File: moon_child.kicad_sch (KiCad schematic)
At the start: 0 parts

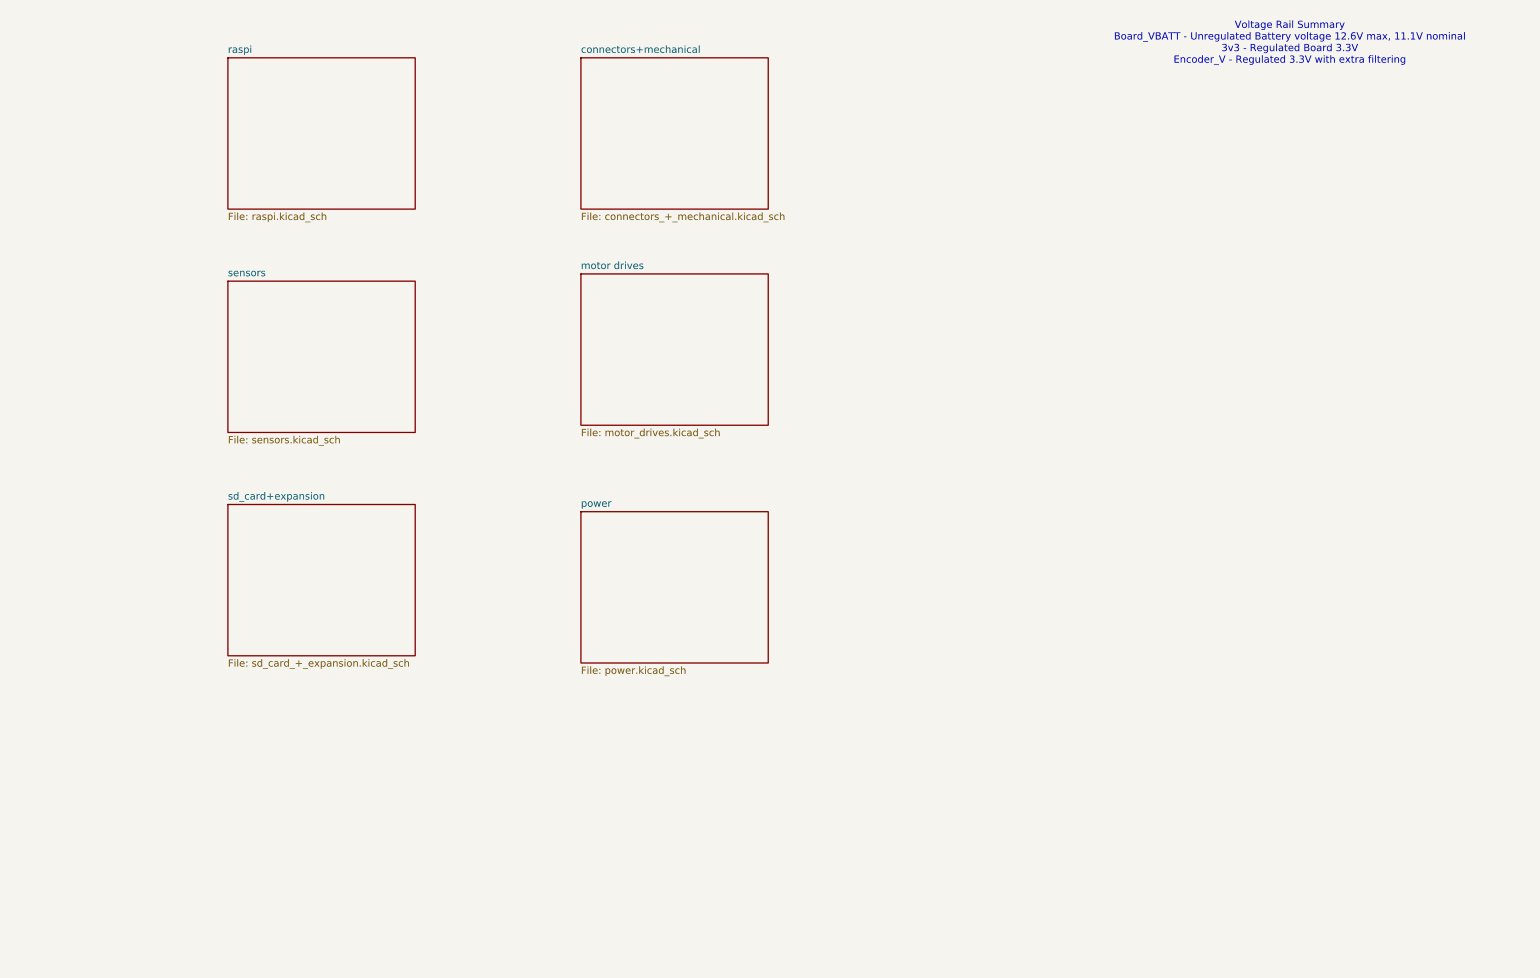
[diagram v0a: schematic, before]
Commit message: Setup top sheet
Added TVS diodes, updated top sheet, misc label fixes
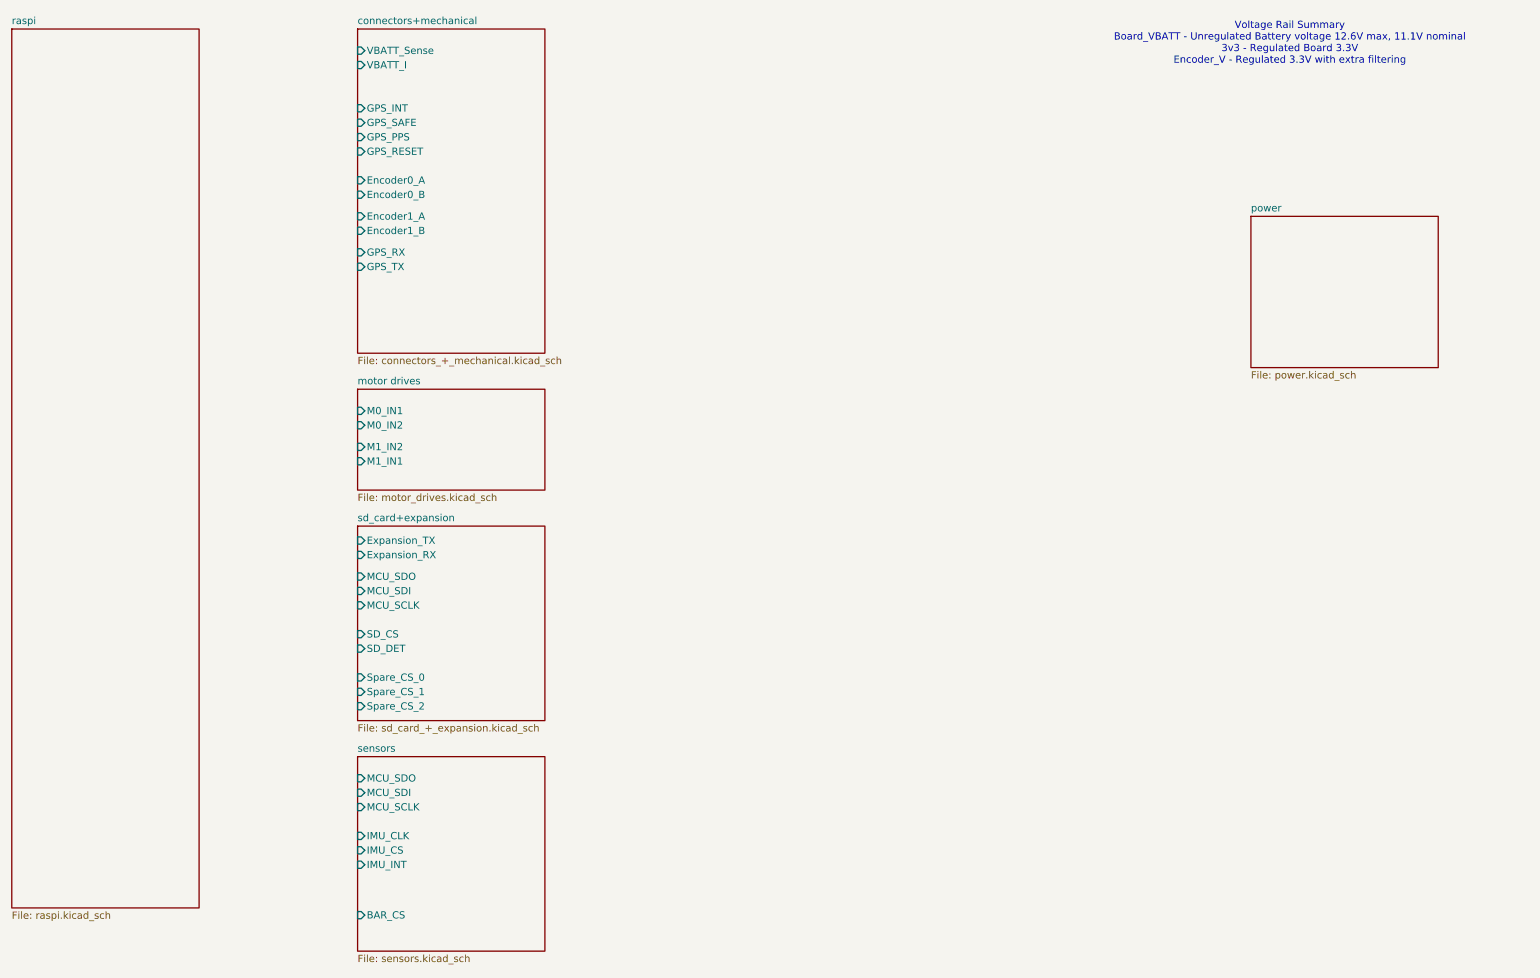
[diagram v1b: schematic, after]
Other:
- sheet connectors+mechanical ports: added Encoder0_A, Encoder0_B, Encoder1_A, Encoder1_B, GPS_INT, GPS_PPS, GPS_RESET, GPS_RX, GPS_SAFE, GPS_TX, VBATT_I, VBATT_Sense; removed none
- sheet motor drives ports: added M0_IN1, M0_IN2, M1_IN1, M1_IN2; removed none
- sheet sd_card+expansion ports: added Expansion_RX, Expansion_TX, MCU_SCLK, MCU_SDI, MCU_SDO, SD_CS, SD_DET, Spare_CS_0, Spare_CS_1, Spare_CS_2; removed none
- sheet sensors ports: added BAR_CS, IMU_CLK, IMU_CS, IMU_INT, MCU_SCLK, MCU_SDI, MCU_SDO; removed none

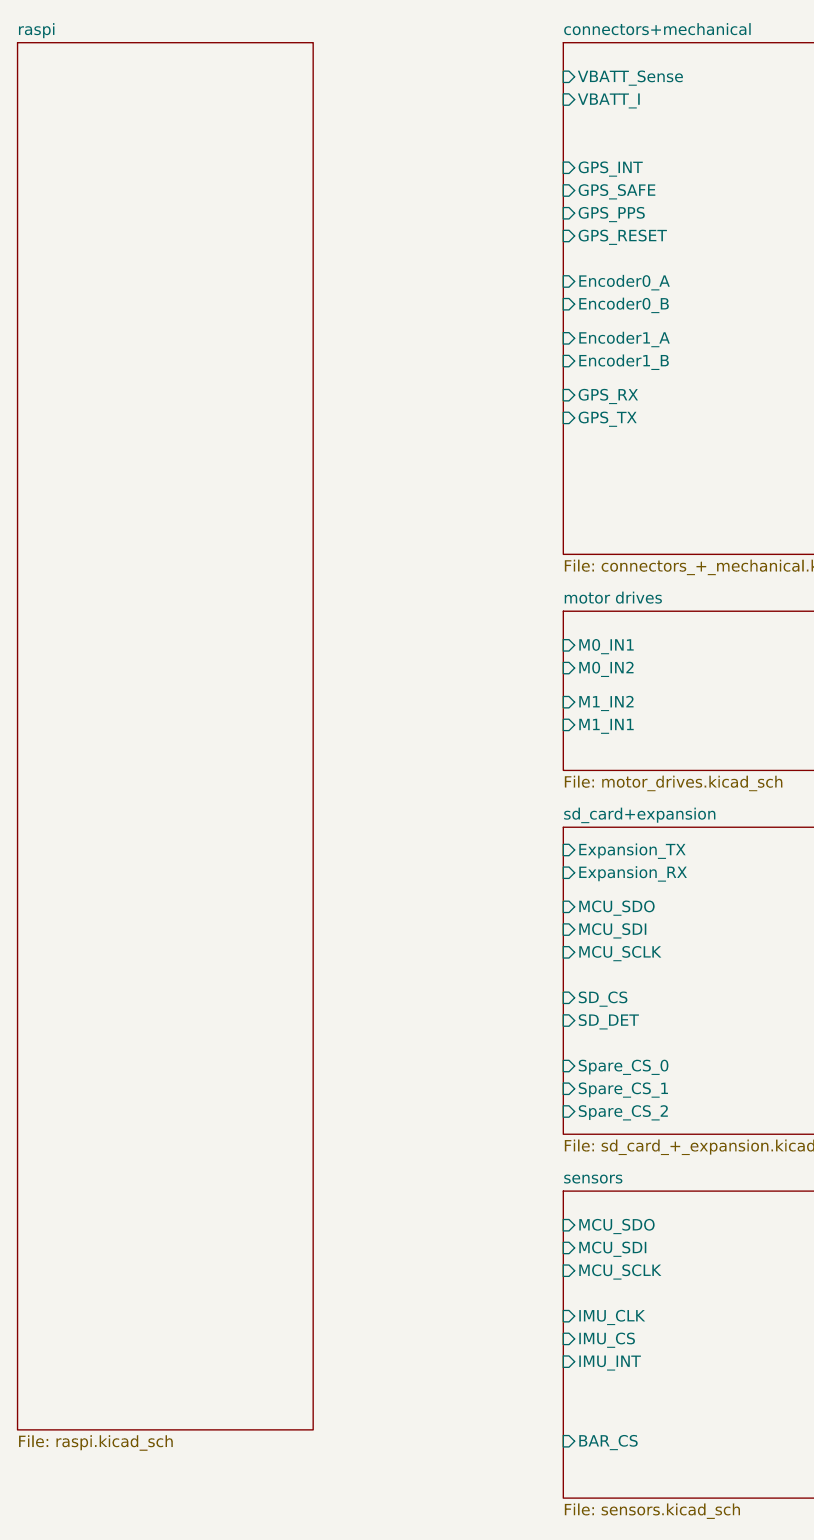
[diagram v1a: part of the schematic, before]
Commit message: Updated sheet to sheet pinout
Updated pinouts and cleared ERCs
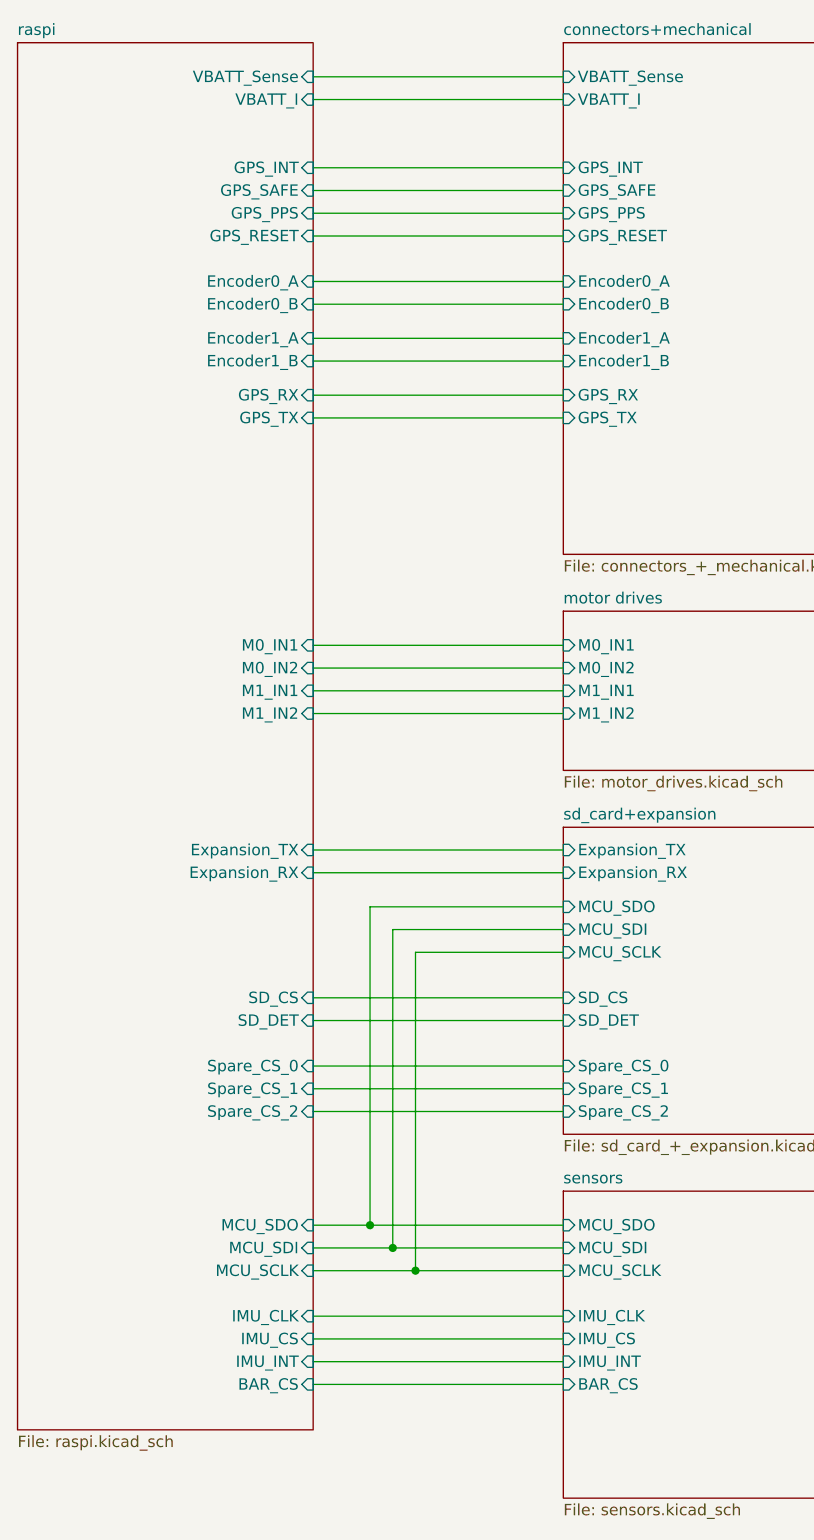
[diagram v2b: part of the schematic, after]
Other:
- sheet raspi ports: added BAR_CS, Encoder0_A, Encoder0_B, Encoder1_A, Encoder1_B, Expansion_RX, Expansion_TX, GPS_INT, GPS_PPS, GPS_RESET, GPS_RX, GPS_SAFE, GPS_TX, IMU_CLK, IMU_CS, IMU_INT, M0_IN1, M0_IN2, M1_IN1, M1_IN2, MCU_SCLK, MCU_SDI, MCU_SDO, SD_CS, SD_DET, Spare_CS_0, Spare_CS_1, Spare_CS_2, VBATT_I, VBATT_Sense; removed none

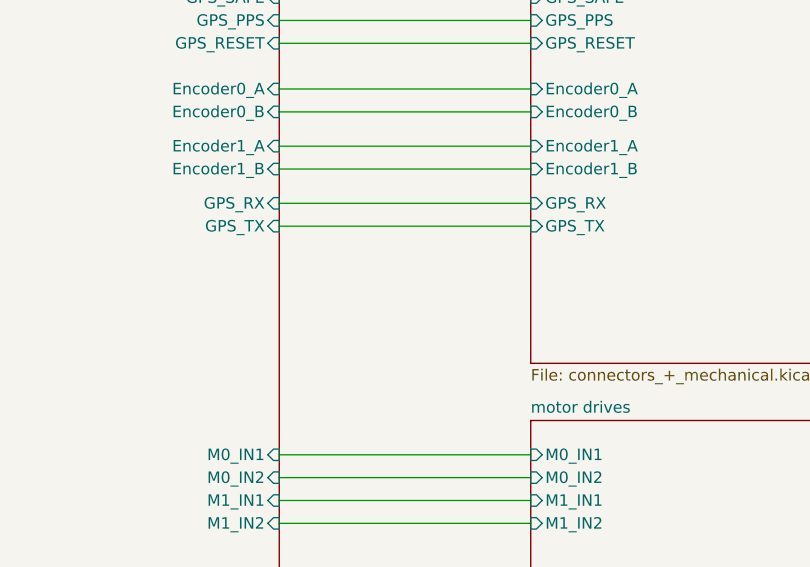
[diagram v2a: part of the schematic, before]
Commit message: Added USB C Connector
Added usb C connector, consolidated ESD parts, cleaned up footprint selection.
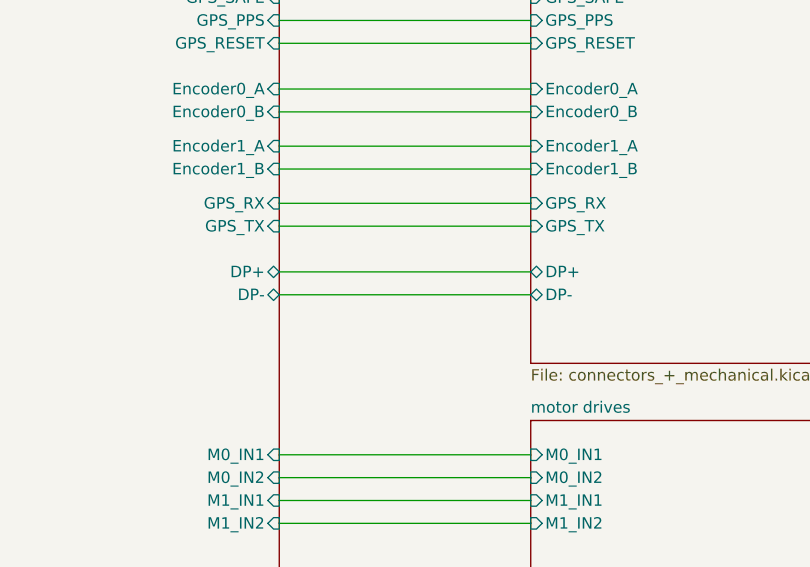
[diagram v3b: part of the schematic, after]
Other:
- sheet connectors+mechanical ports: added DP+, DP-; removed none
- sheet raspi ports: added DP+, DP-; removed none
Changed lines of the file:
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@@
+	(wire
+		(pts
+			(xy 55.88 71.12) (xy 83.82 71.12)
+		)
+		(stroke
+			(width 0)
+			(type default)
+		)
+	)
 	(wire
 		(pts
@@
 		(pts
 			(xy 55.88 27.94) (xy 83.82 27.94)
+		)
+		(stroke
+			(width 0)
+			(type default)
+		)
+	)
+	(wire
+		(pts
+			(xy 55.88 68.58) (xy 83.82 68.58)
 		)
 		(stroke
@@
 			)
 		)
+		(pin "DP+" bidirectional
+			(at 83.82 68.58 180)
+			(effects
+				(font
+					(size 1.27 1.27)
+				)
+				(justify left)
+			)
+		)
+		(pin "DP-" bidirectional
+			(at 83.82 71.12 180)
+			(effects
+				(font
+					(size 1.27 1.27)
+				)
+				(justify left)
+			)
+		)
 		(instances
 			(project "moon_child"
@@
 			(effects
 				(font
+					(size 1.27 1.27)
+				)
+				(justify right)
+			)
+		)
+		(pin "DP+" bidirectional
+			(at 55.88 68.58 0)
+			(effects
+				(font
+					(size 1.27 1.27)
+				)
+				(justify right)
+			)
+		)
+		(pin "DP-" bidirectional
+			(at 55.88 71.12 0)
+			(effects
+				(font

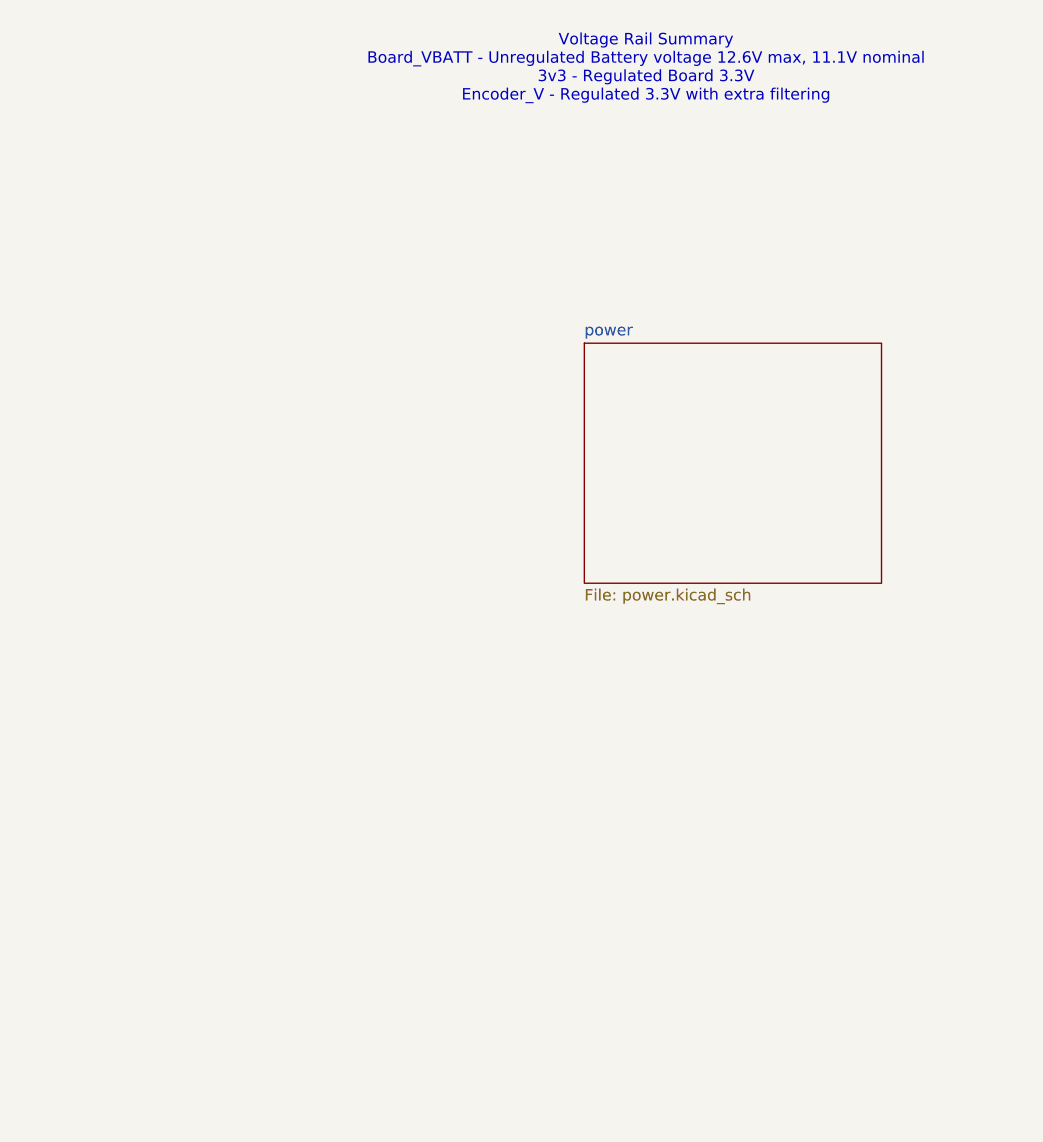
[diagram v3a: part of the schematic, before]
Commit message: Updated layout
Added ground fills, updated stackup, added notes.
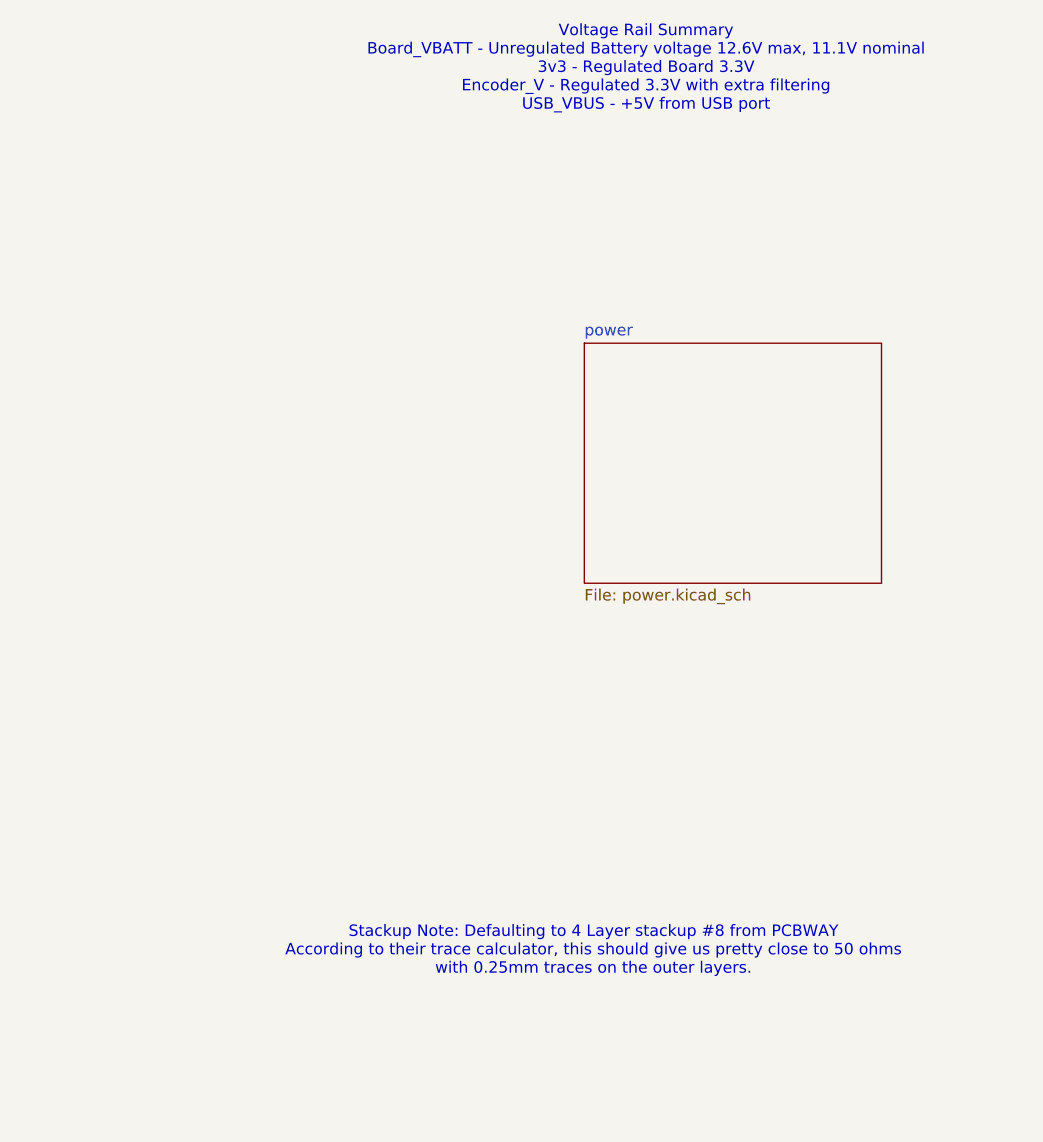
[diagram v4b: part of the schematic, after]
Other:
- note added: "Stackup Note: Defaulting to 4 Layer stackup #8 from PCBWAY According to their trace calculator, this should give us pretty close to 50 ohms with 0.25mm traces on the outer layers."
- note added: "Voltage Rail Summary Board_VBATT - Unregulated Battery voltage 12.6V max, 11.1V nominal 3v3 - Regulated Board 3.3V Encoder_V - Regulated 3.3V with extra filtering USB_VBUS - +5V from USB port"
- note removed: "Voltage Rail Summary Board_VBATT - Unregulated Battery voltage 12.6V max, 11.1V nominal 3v3 - Regulated Board 3.3V Encoder_V - Regulated 3.3V with extra filtering"
